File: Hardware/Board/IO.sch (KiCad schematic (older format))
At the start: 182 parts, among them J7 733-366, J8 734-168, Q200 2N7002, Q201 2N7002, Q202 2N7002, Q203 2N7002, U200 SN74LV4052A, U201 TJA1029T, U202 TJA1029T, U203 TJA1029T, U204 TJA1029T, U205 SN74LV4052A, U206 SN74LV4052A, U207 MAX3072E, U208 MAX3072E, U209 MAX3072E, U210 MAX3072E, U211 MAX11615, U212 PCF8574A, U213 SN65HVD234, U214 DS2482S-800+, U215 SI8422BB-D-IS, U215 SN74LV4052A, U216 SI8422BB-D-IS, U217 SI8422BB-D-IS, U218 SI8422BB-D-IS, U219 USBLC6-2SC6, U220 USBLC6-2SC6, U221 USBLC6-2SC6, U222 USBLC6-2SC6, U224 BTS6143D, U225 BTS6143D, U226 BTS6143D, U227 BTS6143D

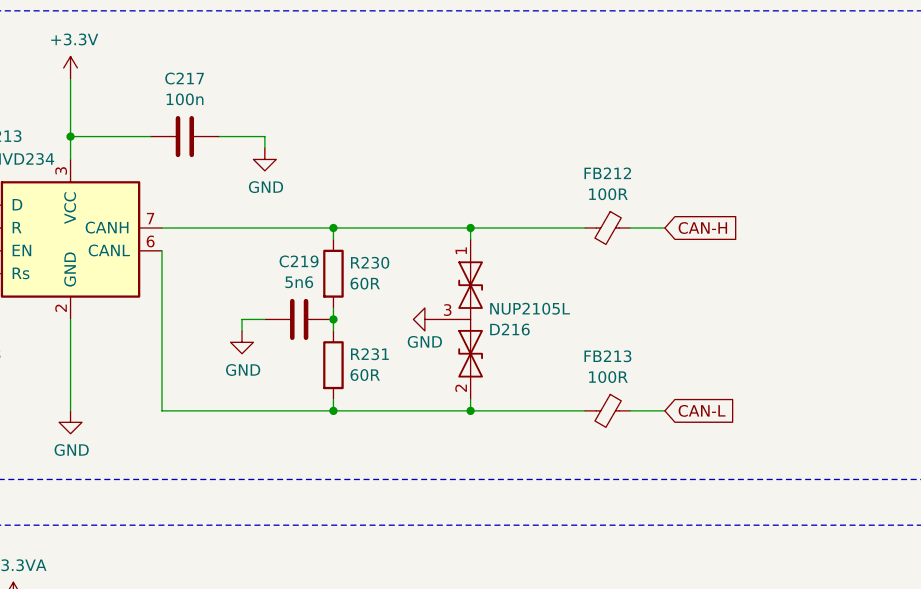
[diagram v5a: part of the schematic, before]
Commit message: Weiter kleinere Anpassungen am CAN und Board
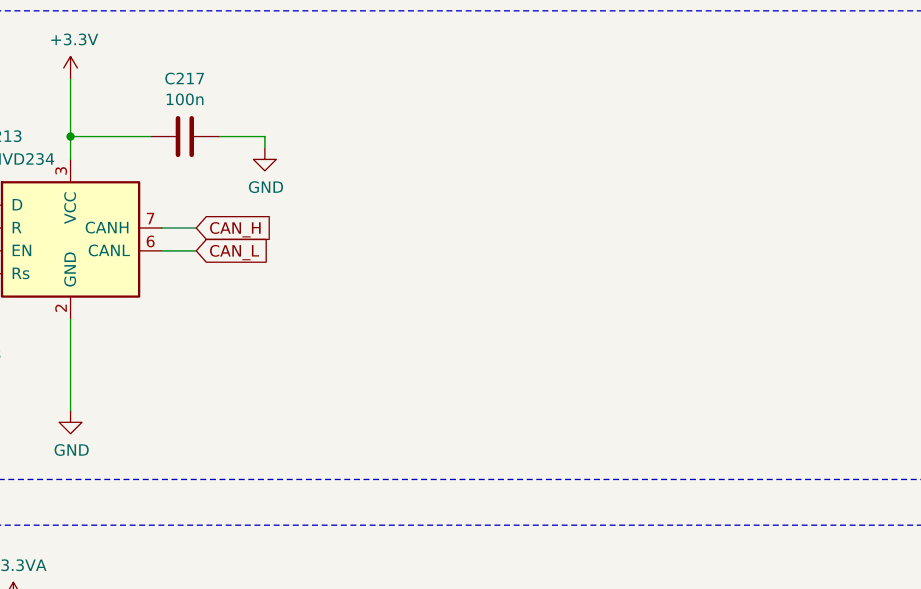
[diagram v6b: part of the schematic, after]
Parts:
- removed C219: 5n6, Capacitor_SMD:C_0603_1608Metric, symbol Womo-rescue:C-Device
- removed D216: NUP2105L, Package_TO_SOT_SMD:SOT-23, symbol Womo-rescue:D_TVS_x2_AAC-Device
- removed FB212, FB213: 100R, Inductor_SMD:L_0603_1608Metric, symbol Womo-rescue:Ferrite_Bead_Small-Device
- removed R230, R231: 60R, Resistor_SMD:R_0603_1608Metric, symbol Womo-rescue:R-Device
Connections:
- net CAN_H: now reaches U213.7 (CANH)
- net CAN_L: now reaches U213.6 (CANL)
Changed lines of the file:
@@
 	6300 5800 6850 5800
 $Comp
-L Womo-rescue:D_TVS_x2_AAC-Device D216
-U 1 1 5CA046D0
-P 14250 6150
-F 0 "D216" V 14296 6229 50  0000 L CNN
-F 1 "NUP2105L" V 14205 6229 50  0000 L CNN
-F 2 "Package_TO_SOT_SMD:SOT-23" H 14100 6150 50  0001 C CNN
-F 3 "~" H 14100 6150 50  0001 C CNN
-	1    14250 6150
-	0    1    1    0
-$EndComp
-$Comp
-L Womo-rescue:R-Device R230
-U 1 1 5CA09C3A
-P 13650 5950
-F 0 "R230" H 13720 5996 50  0000 L CNN
-F 1 "60R" H 13720 5905 50  0000 L CNN
-F 2 "Resistor_SMD:R_0603_1608Metric" V 13580 5950 50  0001 C CNN
-F 3 "~" H 13650 5950 50  0001 C CNN
-	1    13650 5950
-	1    0    0    -1
-$EndComp
-$Comp
-L Womo-rescue:R-Device R231
-U 1 1 5CA09D45
-P 13650 6350
-F 0 "R231" H 13720 6396 50  0000 L CNN
-F 1 "60R" H 13720 6305 50  0000 L CNN
-F 2 "Resistor_SMD:R_0603_1608Metric" V 13580 6350 50  0001 C CNN
-F 3 "~" H 13650 6350 50  0001 C CNN
-	1    13650 6350
-	1    0    0    -1
-$EndComp
-$Comp
 L Womo-rescue:R-Device R215
 U 1 1 5CA11A13
@@
 Wire Wire Line
 	6250 11400 6250 12000
-$Comp
-L Womo-rescue:C-Device C219
-U 1 1 5CA2DCD5
-P 13500 6150
-F 0 "C219" V 13248 6150 50  0000 C CNN
-F 1 "5n6" V 13339 6150 50  0000 C CNN
-F 2 "Capacitor_SMD:C_0603_1608Metric" H 13538 6000 50  0001 C CNN
-F 3 "~" H 13500 6150 50  0001 C CNN
-	1    13500 6150
-	0    1    1    0
-$EndComp
-$Comp
-L Womo-rescue:GND-power #PWR0152
-U 1 1 5CA33685
-P 13250 6200
-F 0 "#PWR0152" H 13250 5950 50  0001 C CNN
-F 1 "GND" H 13255 6027 50  0000 C CNN
-F 2 "" H 13250 6200 50  0001 C CNN
-F 3 "" H 13250 6200 50  0001 C CNN
-	1    13250 6200
-	1    0    0    -1
-$EndComp
-Wire Wire Line
-	14250 5750 14250 5800
-Wire Wire Line
-	13650 5800 13650 5750
-Connection ~ 13650 5750
-Wire Wire Line
-	13650 5750 14250 5750
-Wire Wire Line
-	13650 6100 13650 6150
-Wire Wire Line
-	13650 6200 13650 6150
-Connection ~ 13650 6150
-Wire Wire Line
-	13350 6150 13250 6150
-Wire Wire Line
-	13250 6150 13250 6200
-Wire Wire Line
-	14250 6500 14250 6550
-Wire Wire Line
-	14250 6550 13650 6550
-Wire Wire Line
-	13650 6500 13650 6550
-Connection ~ 13650 6550
-Text GLabel 15100 5750 2    50   Input ~ 0
-CAN-H
-Text GLabel 15100 6550 2    50   Input ~ 0
-CAN-L
-Wire Wire Line
-	14750 5750 14250 5750
-Connection ~ 14250 5750
-Wire Wire Line
-	14750 6550 14250 6550
-Connection ~ 14250 6550
+Text GLabel 13050 5750 2    50   Input ~ 0
+CAN_H
+Text GLabel 13050 5850 2    50   Input ~ 0
+CAN_L
 $Comp
 L Womo-rescue:D_TVS-Device D201
@@
 Wire Wire Line
 	7700 5800 7600 5800
-$Comp
-L Womo-rescue:Ferrite_Bead_Small-Device FB212
-U 1 1 5CBB38BB
-P 14850 5750
-F 0 "FB212" V 14613 5750 50  0000 C CNN
-F 1 "100R" V 14704 5750 50  0000 C CNN
-F 2 "Inductor_SMD:L_0603_1608Metric" V 14780 5750 50  0001 C CNN
-F 3 "~" H 14850 5750 50  0001 C CNN
-	1    14850 5750
-	0    1    1    0
-$EndComp
-$Comp
-L Womo-rescue:Ferrite_Bead_Small-Device FB213
-U 1 1 5CBB7155
-P 14850 6550
-F 0 "FB213" V 14613 6550 50  0000 C CNN
-F 1 "100R" V 14704 6550 50  0000 C CNN
-F 2 "Inductor_SMD:L_0603_1608Metric" V 14780 6550 50  0001 C CNN
-F 3 "~" H 14850 6550 50  0001 C CNN
-	1    14850 6550
-	0    1    1    0
-$EndComp
 Wire Wire Line
-	15100 5750 14950 5750
+	13050 5750 12900 5750
 Wire Wire Line
-	15100 6550 14950 6550
+	13050 5850 12900 5850
 $Comp
 L Womo-rescue:Ferrite_Bead_Small-Device FB206
@@
 	0    1    1    0
 $EndComp
-$Comp
-L Womo-rescue:GND-power #PWR0151
-U 1 1 5E07C1D9
-P 14100 6150
-F 0 "#PWR0151" H 14100 5900 50  0001 C CNN
-F 1 "GND" V 14200 6100 50  0000 C CNN
-F 2 "" H 14100 6150 50  0001 C CNN
-F 3 "" H 14100 6150 50  0001 C CNN
-	1    14100 6150
-	0    1    1    0
-$EndComp
 Wire Wire Line
 	7700 2000 7600 2000
@@
 $EndComp
 Wire Wire Line
-	12900 5750 13650 5750
-Wire Wire Line
-	12900 5850 12900 6550
-Wire Wire Line
-	12900 6550 13650 6550
-Wire Wire Line
 	12500 6150 12500 6550

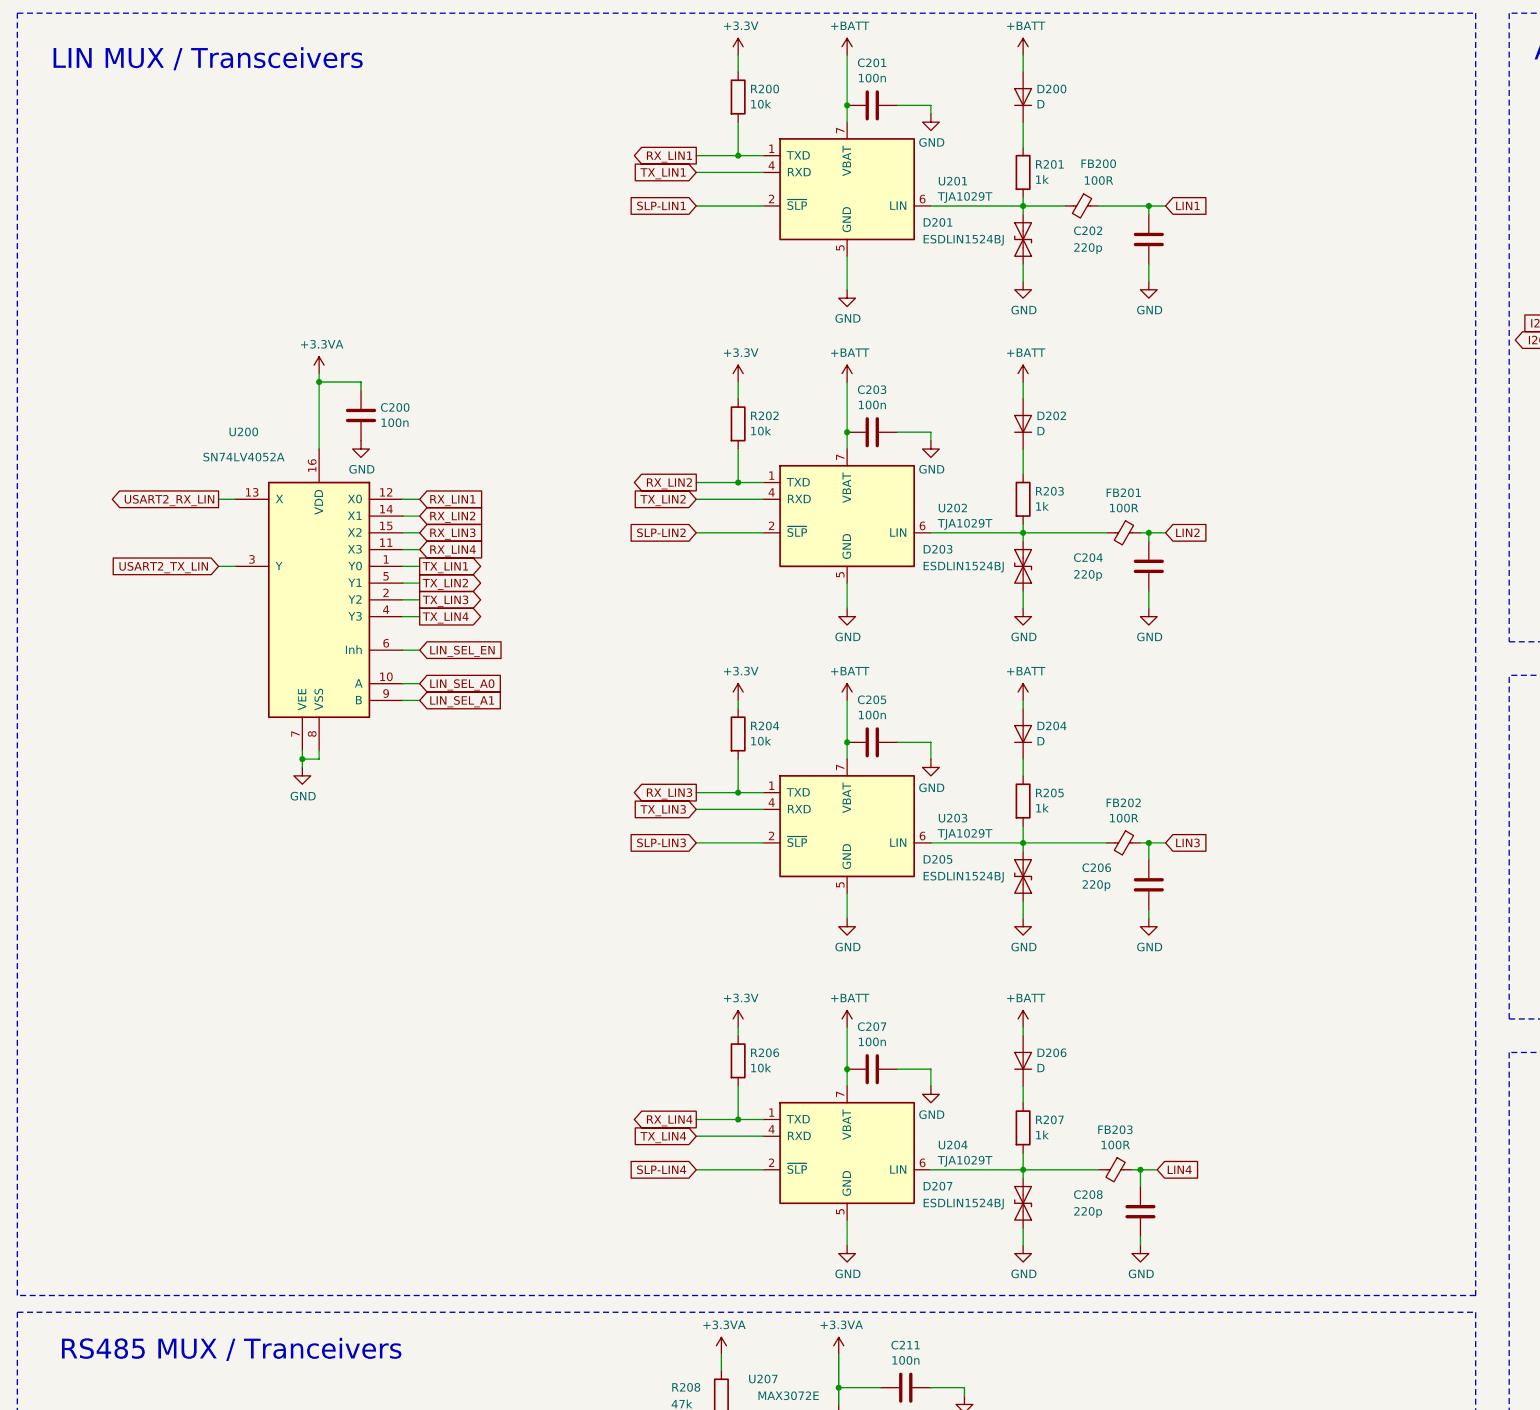
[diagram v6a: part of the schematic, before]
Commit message: Weiter Änderungen Schaltplan, freien UART auf Truma LIN, Grobes Placement Schaltplan
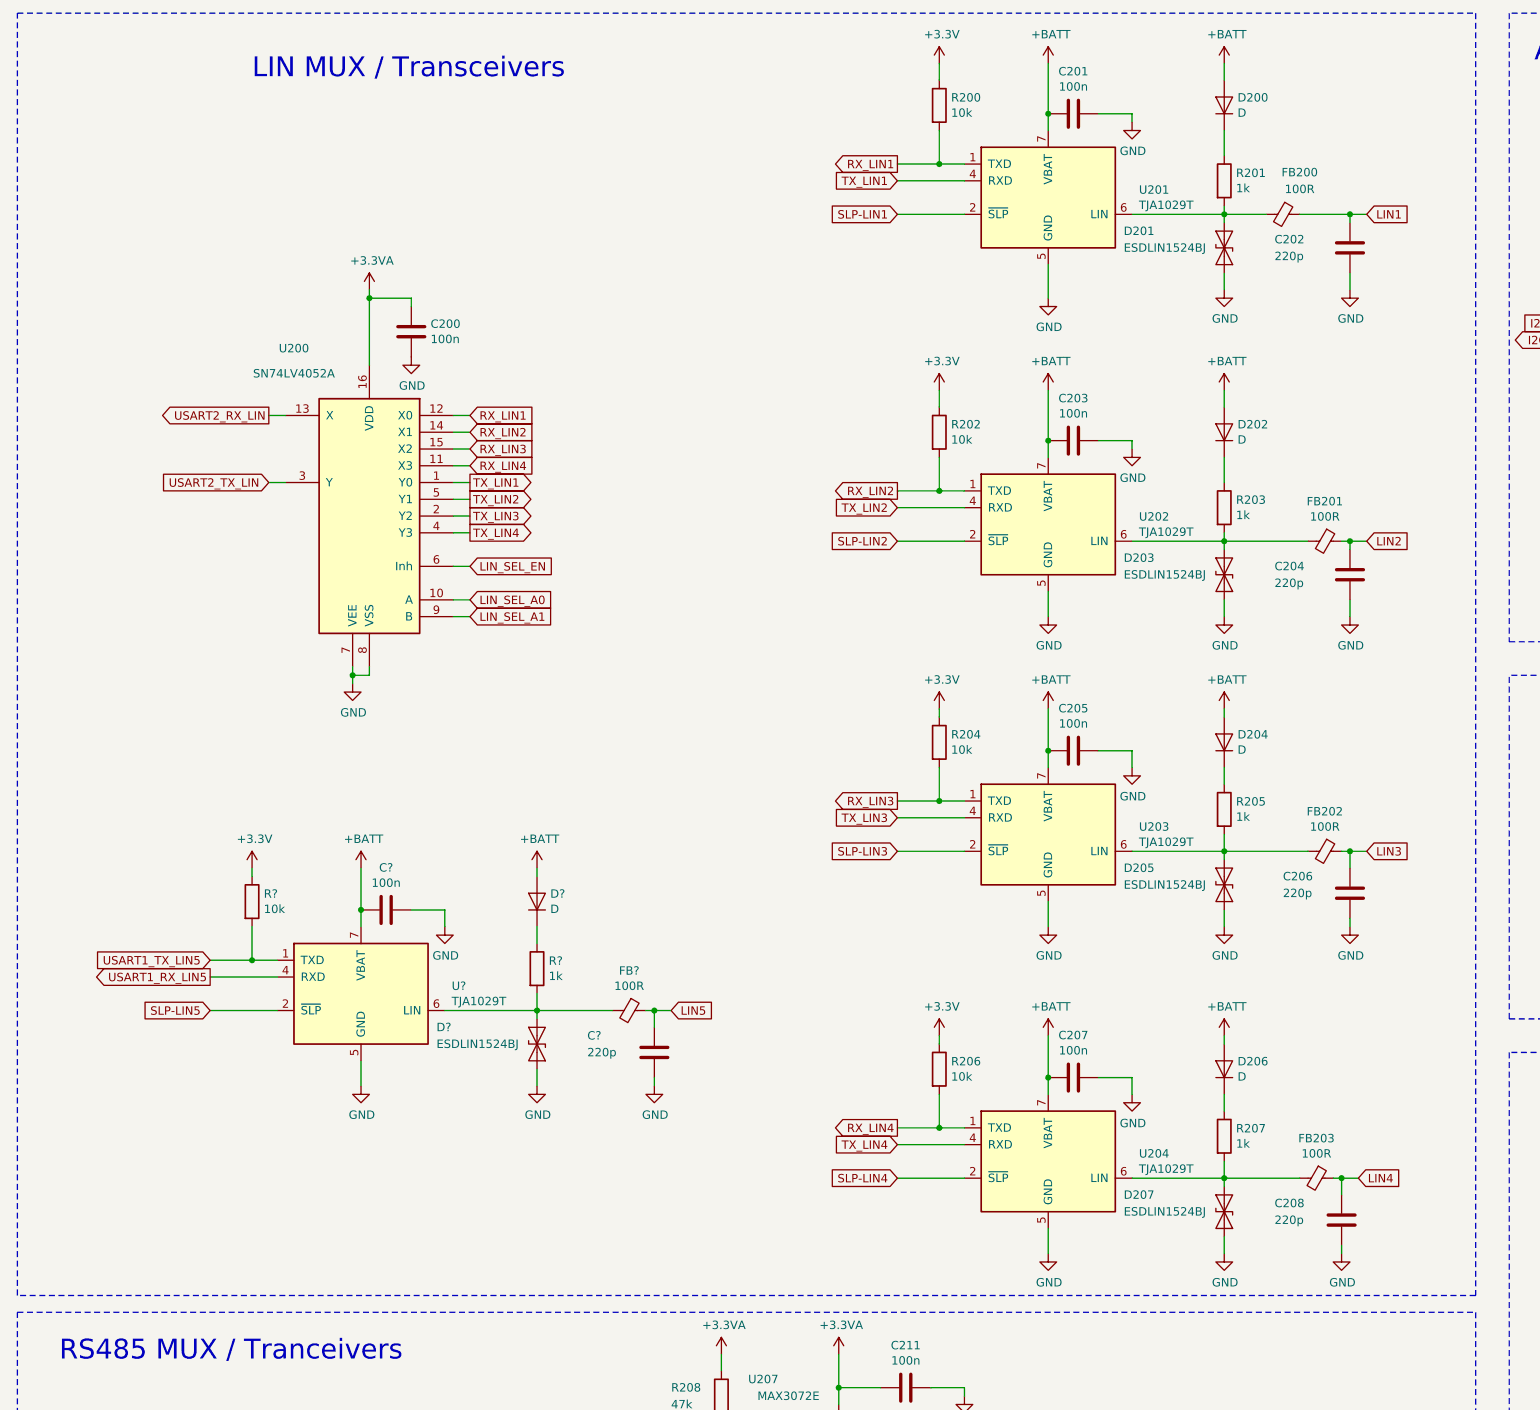
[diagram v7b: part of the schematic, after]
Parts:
- added C?: 100n, Capacitor_SMD:C_0603_1608Metric, symbol Womo-rescue:C-Device
- added C?: 220p, Capacitor_SMD:C_0603_1608Metric, symbol Womo-rescue:C-Device
- added D?: D, Diode_SMD:D_SOD-323, symbol Womo-rescue:D-Device
- added D?: ESDLIN1524BJ, Diode_SMD:D_SOD-323, symbol Womo-rescue:D_TVS-Device
- added FB?: 100R, Inductor_SMD:L_0603_1608Metric, symbol Womo-rescue:Ferrite_Bead_Small-Device
- added R?: 1k, Resistor_SMD:R_0603_1608Metric, symbol Womo-rescue:R-Device
- added R?: 10k, Resistor_SMD:R_0603_1608Metric, symbol Womo-rescue:R-Device
- added U?: TJA1029T, Package_SO:SOIC-8_3.9x4.9mm_P1.27mm, symbol Womo-rescue:TJA1029T-Interface_CAN_LIN
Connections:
- net +3V3: now also R?.1
- net +BATT: now also C?.2, D?.2 (A), U?.7 (VBAT)
- net GND: now also C?.1, C?.2, D?.2 (A2), U?.5 (GND)
- new net: D?.1 (A1), FB?.2, R?.2, U?.6 (LIN)
- new net: D?.1 (K), R?.1
- new net LIN5: C?.1, FB?.1
- new net SLP-LIN5: U?.2 (~SLP~)
- new net USART1_RX_LIN5: U?.4 (RXD)
- new net USART1_TX_LIN5: R?.2, U?.1 (TXD)
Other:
- moved on the sheet: C200, C201, C202, C203, C204, C205, C206, C207, C208, D200, D201, D202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
